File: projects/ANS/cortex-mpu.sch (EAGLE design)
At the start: 26 parts, among them IC1 LM1117MPX-3.3, U1 AT32UC3B164-AUT, Y1 7A-16

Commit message: mpu
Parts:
- added C10, C8: 0.1uF, SparkFun-Passives:CAP0603-CAP
- added C11: 10nF, SparkFun-Passives:CAP0603-CAP
- added C9: 2.2nF, SparkFun-Passives:CAP0603-CAP
- added CLKOUT, E_SCL, E_SDA: (no value), wirepad:1,6/0,8
- added D2, D6: GREEN, SparkFun-LED:LED-GREEN0603
- added LOGO1: OSHW-LOGOS-COPPER, SparkFun-Aesthetics:OSHW-LOGOS-COPPER
- added R10, R9: 150R, SparkFun-Passives:RESISTOR0603-RES
- added R11, R12: 10kR, SparkFun-Passives:RESISTOR0603-RES
- added SJ1, SJ2: SPK, SparkFun-Passives:JUMPER-PAD-2-NC_BY_TRACE
- added SJ3: SPK, SparkFun-Passives:JUMPER-PAD-3-2OF3_NC_BY_TRACE_LARGE
- added U2: (no value), SparkFun-Sensors:MPU-9150QFN-24-NP
- D5: value RED -> GREEN; device SparkFun-LED:LED-RED0603 -> SparkFun-LED:LED-GREEN0603
- R5, R6: value 820R -> 150R
- R7: value (none) -> 150R
- S1: value SWITCH-MOMENTARY-2SMD-4 -> 2SMD-4
- S2: value SWITCH-MOMENTARY-2SMD-4 -> 2SMD4
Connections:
- new net E_SDA: E_SDA.P, U2.E_SDA
- new net GNDANA: U1.GNDANA
- new net N$10: C8.1, U2.REGOUT
- new net N$11: C9.1, U2.CPOUT
- new net N$12: SJ3.2, U2.AD0
- new net N$14: E_SCL.P, U2.E_SCL
- new net N$15: SJ1.2, U2.FSYNC
- new net N$16: CLKOUT.P, U2.CLKOUT
- new net N$6: D5.A, R7.1
- new net N$7: D6.A, R9.1
- new net N$8: D2.A, R10.1
- new net N$9: SJ2.2, U2.CLKIN
- new net VDDANA: U1.VDDANA
- new net VDDCORE: U1.VDDCORE
- new net VDDCORE_2: U1.VDDCORE_2
- new net VDDCORE_3: U1.VDDCORE_3
- new net VDDIN: U1.VDDIN
- new net VDDIO: U1.VDDIO
- new net VDDIO_2: U1.VDDIO_2
- new net VDDIO_3: U1.VDDIO_3
- new net VDDOUT: U1.VDDOUT
- new net VDDPLL: U1.VDDPLL
- net GND: now also C10.2, C11.2, C8.2, C9.2, SJ1.1, SJ2.1, SJ3.3, U2.GND@15, U2.GND@17, U2.GND@18
- net PA10: now also R12.1, U2.SDA
- net PA21: now also D5.C
- net PA22: now also D6.C
- net PA5: now also U2.INT
- net PA7: now also D2.C
- net PA9: now also R11.1, U2.SCL
- net VCC: now also C10.1, C11.1, R10.2, R11.2, R12.2, R7.2, R9.2, SJ3.1, U2.VDD@13, U2.VDD@3, U2.VLOGIC
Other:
- note added: "MPU-9150 I2C/TWI"
- moved on the sheet: C6, C7, D3, D4, D5, R3, R4, R5, R6, R7, S1, S2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

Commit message: vdd
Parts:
- added L1: 3.3uH, SparkFun-Passives:INDUCTOR0603
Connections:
- removed net VDDIO_2: U1.VDDIO_2
- removed net VDDIO_3: U1.VDDIO_3
- net VCC: now also L1.1
- net VDDANA: now also L1.2, U1.ADVREF
- net VDDIO: now also U1.VDDIO_2, U1.VDDIO_3
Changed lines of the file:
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@@
 <part name="GND9" library="SparkFun-Aesthetics" deviceset="GND" device=""/>
 <part name="LOGO1" library="SparkFun-Aesthetics" deviceset="OSHW-LOGO" device="S-COPPER"/>
+<part name="L1" library="SparkFun-Passives" deviceset="INDUCTOR" device="0603" value="3.3uH"/>
+<part name="SUPPLY1" library="SparkFun-Aesthetics" deviceset="VCC" device=""/>
 </parts>
 <sheets>
@@
 <instance part="GND9" gate="1" x="142.24" y="10.16"/>
 <instance part="LOGO1" gate="G$1" x="162.56" y="12.7"/>
+<instance part="L1" gate="G$1" x="12.7" y="43.18"/>
+<instance part="SUPPLY1" gate="G$1" x="12.7" y="53.34"/>
 </instances>
 <busses>
@@
 <wire x1="60.96" y1="38.1" x2="63.5" y2="38.1" width="0.1524" layer="91"/>
 </segment>
+<segment>
+<pinref part="SUPPLY1" gate="G$1" pin="VCC"/>
+<pinref part="L1" gate="G$1" pin="1"/>
+<wire x1="12.7" y1="53.34" x2="12.7" y2="50.8" width="0.1524" layer="91"/>
+</segment>
 </net>
 <net name="N$5" class="0">
@@
 <segment>
 <pinref part="U1" gate="A" pin="VDDANA"/>
-<wire x1="35.56" y1="170.18" x2="30.48" y2="170.18" width="0.1524" layer="91"/>
+<wire x1="35.56" y1="170.18" x2="33.02" y2="170.18" width="0.1524" layer="91"/>
 <label x="20.32" y="170.18" size="1.778" layer="95"/>
+<wire x1="33.02" y1="170.18" x2="30.48" y2="170.18" width="0.1524" layer="91"/>
+<wire x1="33.02" y1="170.18" x2="33.02" y2="142.24" width="0.1524" layer="91"/>
+<junction x="33.02" y="170.18"/>
+<pinref part="U1" gate="A" pin="ADVREF"/>
+<wire x1="33.02" y1="142.24" x2="35.56" y2="142.24" width="0.1524" layer="91"/>
+</segment>
+<segment>
+<wire x1="12.7" y1="33.02" x2="12.7" y2="35.56" width="0.1524" layer="91"/>
+<pinref part="L1" gate="G$1" pin="2"/>
+<label x="7.62" y="33.02" size="1.778" layer="95"/>
 </segment>
 </net>
@@
 <wire x1="35.56" y1="160.02" x2="30.48" y2="160.02" width="0.1524" layer="91"/>
 <label x="20.32" y="160.02" size="1.778" layer="95"/>
-</segment>
-</net>
-<net name="VDDIO_2" class="0">
-<segment>
-<pinref part="U1" gate="A" pin="VDDIO_2"/>
-<wire x1="35.56" y1="157.48" x2="30.48" y2="157.48" width="0.1524" layer="91"/>
-<label x="20.32" y="157.48" size="1.778" layer="95"/>
-</segment>
-</net>
-<net name="VDDIO_3" class="0">
-<segment>
-<pinref part="U1" gate="A" pin="VDDIO_3"/>
-<wire x1="35.56" y1="154.94" x2="30.48" y2="154.94" width="0.1524" layer="91"/>
-<label x="20.32" y="154.94" size="1.778" layer="95"/>
-</segment>
-</net>
-<net name="VDDIO" class="0">
-<segment>
-<pinref part="U1" gate="A" pin="VDDIO"/>
-<wire x1="35.56" y1="152.4" x2="30.48" y2="152.4" width="0.1524" layer="91"/>
-<label x="20.32" y="152.4" size="1.778" layer="95"/>
 </segment>
 </net>
@@
 </segment>
 </net>
+<net name="VDDIO" class="0">
+<segment>
+<pinref part="U1" gate="A" pin="VDDIO_2"/>
+<wire x1="35.56" y1="157.48" x2="30.48" y2="157.48" width="0.1524" layer="91"/>
+<pinref part="U1" gate="A" pin="VDDIO_3"/>
+<wire x1="35.56" y1="154.94" x2="30.48" y2="154.94" width="0.1524" layer="91"/>
+<label x="20.32" y="154.94" size="1.778" layer="95"/>
+<wire x1="30.48" y1="157.48" x2="30.48" y2="154.94" width="0.1524" layer="91"/>
+<pinref part="U1" gate="A" pin="VDDIO"/>
+<wire x1="35.56" y1="152.4" x2="30.48" y2="152.4" width="0.1524" layer="91"/>
+<wire x1="30.48" y1="154.94" x2="30.48" y2="152.4" width="0.1524" layer="91"/>
+<junction x="30.48" y="154.94"/>
+</segment>
+</net>

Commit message: Decoupling
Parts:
- added C12, C13, C14, C15, C16, C17, C18, C19, C20, C21, C22, C23, C24, C25, C26, C27, C28, C29, C30, C31, C32, C33, C34: (no value), SparkFun-Passives:CAP0603-CAP
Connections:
- net GND: now also C12.2, C13.2, C14.2, C15.2, C16.2, C17.2, C18.2, C19.2, C20.2, C21.2, C22.2, C23.2, C24.2, C25.2, C26.2, C27.2, C28.2, C29.2, C30.2, C31.2, C32.2, C33.2, C34.2
- net VDDCORE: now also C25.1, C26.1, C27.1, C28.1, C29.1, C30.1, C31.1, C32.1, C33.1, C34.1
- net VDDIN: now also C23.1, C24.1
- net VDDIO: now also C15.1, C16.1, C17.1, C18.1, C19.1, C20.1
- net VDDOUT: now also C21.1, C22.1
- net VDDPLL: now also C12.1, C13.1, C14.1
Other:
- note added: "Decoupling Capacitors"
- note added: "Filter"
- moved on the sheet: C10, C11, C8, C9, CLKOUT, E_SCL, E_SDA, L1, R11, R12, SJ1, SJ2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

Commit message: Decoupling Capr
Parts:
- added C35: 4.7uF, SparkFun-Passives:CAP0603-CAP
- added C36: 100nF, SparkFun-Passives:CAP0603-CAP
- added C37: 33nF, SparkFun-Passives:CAP0603-CAP
- C12, C25, C26, C27: value (none) -> 2.7nF
- C13, C18, C19, C20, C23, C28, C29, C30: value (none) -> 33nF
- C14: value (none) -> 2.2nF
- C15, C16, C17, C24, C31, C32, C33: value (none) -> 100nF
- C21, C34: value (none) -> 2.2uF
- C22: value (none) -> 470pF
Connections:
- removed net GNDANA: U1.GNDANA
- net GND: now also C35.2, C36.2, C37.2, U1.GNDANA
- net VDDANA: now also C36.1, C37.1
- net VDDIO: now also C35.1
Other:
- moved on the sheet: C10, C11, C18, C19, C20, C8, C9, CLKOUT, E_SCL, E_SDA, R11, R12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

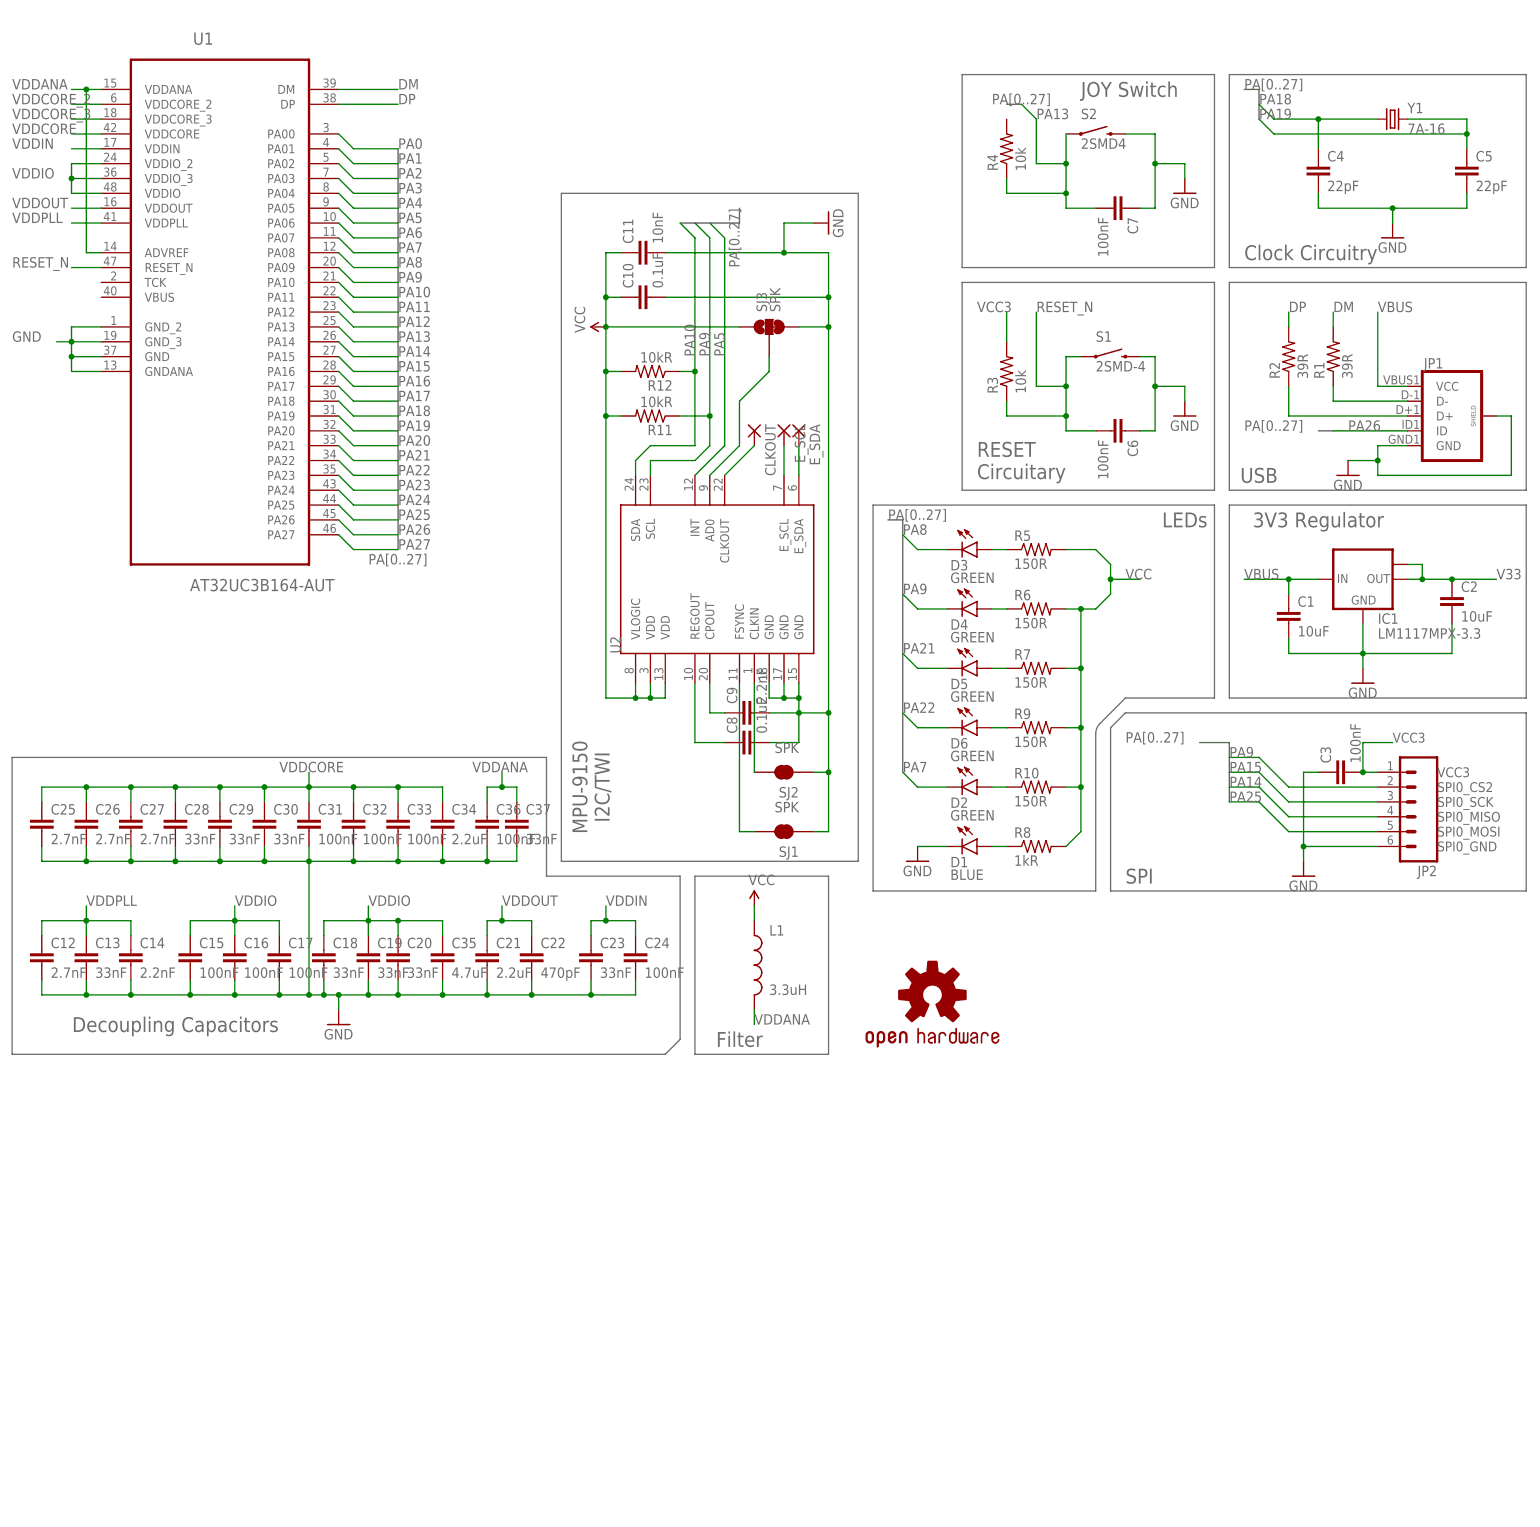
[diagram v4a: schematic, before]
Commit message: Decoupling, Changes
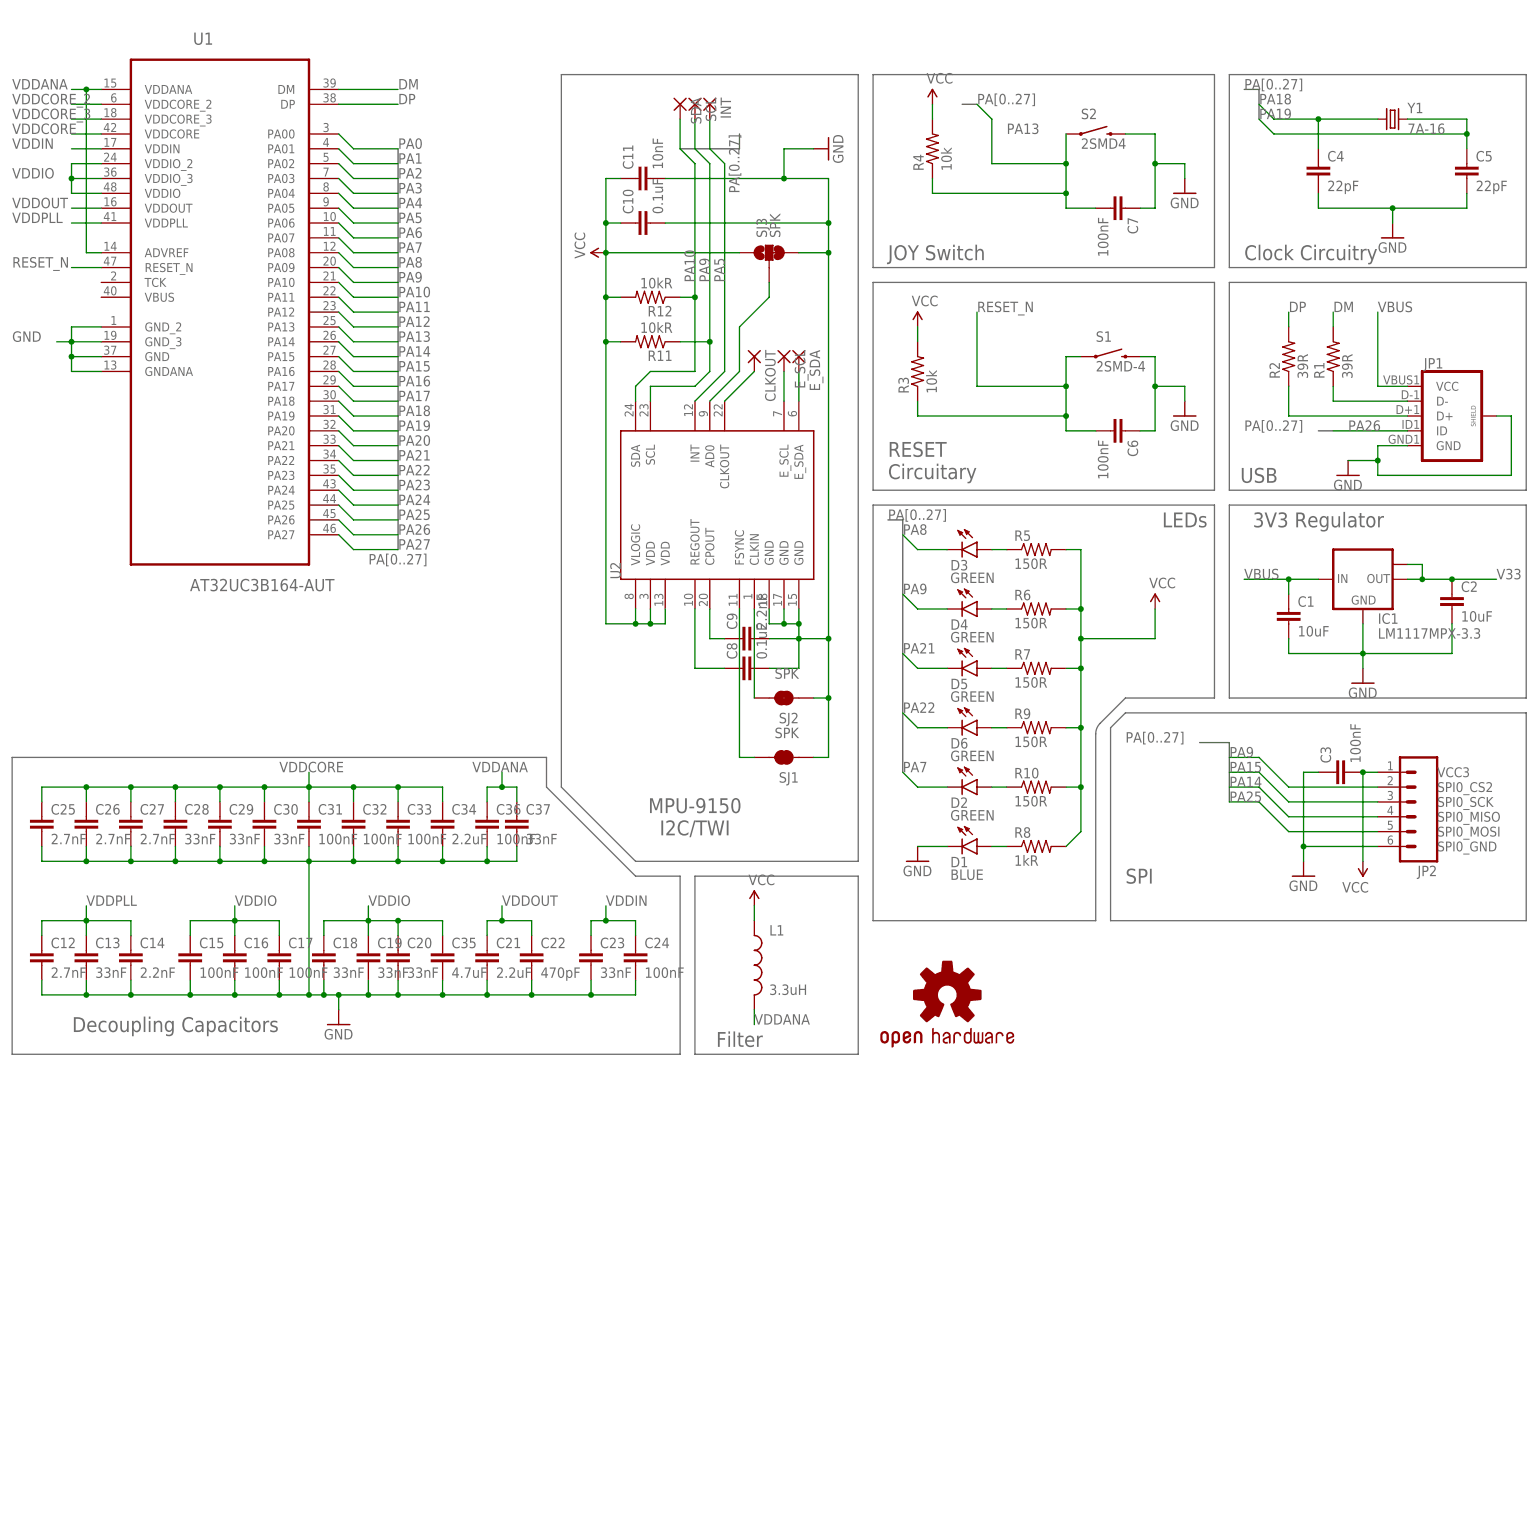
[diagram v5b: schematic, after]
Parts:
- added INT, SCL, SDA: (no value), wirepad:1,6/0,8
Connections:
- removed net VCC3: C3.2, JP2.1, R3.2
- net PA10: now also SDA.P
- net PA5: now also INT.P
- net PA9: now also SCL.P
- net VCC: now also C3.2, JP2.1, R3.2, R4.2
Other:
- moved on the sheet: C10, C11, C8, C9, CLKOUT, E_SCL, E_SDA, R11, R12, R3, R4, SJ1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

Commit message: Pdf
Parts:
- C1, C2: value 10uF -> 2.7nF
- C10, C8: value 0.1uF -> 100nF
- C11: value 10nF -> 33nF
- C12, C26: value 2.7nF -> 100nF
- C13: value 33nF -> 100nF
- C14, C9: value 2.2nF -> 33nF
- C16, C7: value 100nF -> 33nF
- C19: value 33nF -> 2.2uF
- C20: value 33nF -> 4.7uF
- C21: value 2.2uF -> 100nF
- C22: value 470pF -> 2.2uF
- C24: value 100nF -> 470pF
- C25: value 2.7nF -> 33nF
- C27: value 2.7nF -> 10nF
- C28, C30: value 33nF -> 0.1uF
- C29: value 33nF -> 2.2nF
- C3: value 100nF -> 2.7nF
- C33, C36: value 100nF -> 10uF
- C34: value 2.2uF -> 22pF
- C35: value 4.7uF -> 100nF
- C37: value 33nF -> 22pF
- C4: value 22pF -> 33nF
- C5: value 22pF -> 2.7nF
- C6: value 100nF -> 2.2nF
- D1: value BLUE -> GREEN; device SparkFun-LED:LED-BLUE0603 -> SparkFun-LED:LED-GREEN0603
- D6: value GREEN -> BLUE; device SparkFun-LED:LED-GREEN0603 -> SparkFun-LED:LED-BLUE0603
- JP1: device SparkFun-Connectors:USB_MICROB_PLUGCONN-11752 -> SparkFun-Connectors:M06LOCK_LONGPADS
- JP2: device SparkFun-Connectors:M06LOCK_LONGPADS -> SparkFun-Connectors:USB_MICROB_PLUGCONN-11752
- R1, R2: value 39R -> 10kR
- R10: value 150R -> 1kR
- R11, R12: value 10kR -> 39R
- R8: value 1kR -> 150R
- S1: value 2SMD-4 -> 2SMD4
- S2: value 2SMD4 -> 2SMD-4
- SJ1: device SparkFun-Passives:JUMPER-PAD-2-NC_BY_TRACE -> SparkFun-Passives:JUMPER-PAD-3-2OF3_NC_BY_TRACE_LARGE
- SJ3: device SparkFun-Passives:JUMPER-PAD-3-2OF3_NC_BY_TRACE_LARGE -> SparkFun-Passives:JUMPER-PAD-2-NC_BY_TRACE
- renumbered CLKOUT to PAD4, E_SCL to PAD5, E_SDA to PAD6, INT to PAD3, SCL to PAD2, SDA to PAD1
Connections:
- net DM: now also R12.2; no longer R1.2
- net DP: now also R11.2; no longer R2.2
- net GND: now also C3.2, C31.1, C32.1, C35.1, C6.2, C7.2, D6.C, JP1.6, JP2.GND, JP2.SHIELD, SJ1.3, SJ3.1; no longer C3.1, C31.2, C32.2, C35.2, C6.1, C7.1, D1.C, JP1.GND, JP1.SHIELD, JP2.6, SJ1.1, SJ3.3
- net N$1: now also JP2.D-, R12.1; no longer JP1.D-, R1.1
- net N$10: now also C30.1; no longer C8.1
- net N$11: now also C29.1; no longer C9.1
- net N$12: now also SJ1.2; no longer SJ3.2
- net N$15: now also SJ3.2; no longer SJ1.2
- net N$2: now also JP2.D+, R11.1; no longer JP1.D+, R2.1
- net N$3: now also D1.A; no longer D3.A
- net N$4: now also D2.A; no longer D4.A
- net N$5: now also D6.A, R10.1; no longer D1.A, R8.1
- net N$6: now also D3.A; no longer D5.A
- net N$7: now also D4.A, R8.1; no longer D6.A, R9.1
- net N$8: now also D5.A, R9.1; no longer D2.A, R10.1
- net PA10: now also R1.1; no longer R12.1
- net PA13: now also C31.2, S1.1; no longer C7.2, S2.1
- net PA14: now also JP1.4; no longer JP2.4
- net PA15: now also JP1.3; no longer JP2.3
- net PA18: now also C34.1; no longer C4.1
- net PA19: now also C37.1; no longer C5.1
- net PA21: now also D3.C; no longer D5.C
- net PA22: now also D4.C; no longer D6.C
- net PA25: now also JP1.5; no longer JP2.5
- net PA26: now also JP2.ID; no longer JP1.ID
- net PA7: now also D5.C; no longer D2.C
- net PA8: now also D1.C; no longer D3.C
- net PA9: now also D2.C, JP1.2, R2.1; no longer D4.C, JP2.2, R11.1
- net RESET_N: now also C32.2, S2.1; no longer C6.2, S1.1
- net V33: now also C36.1; no longer C2.1
- net VBUS: now also C33.1, JP2.VCC; no longer C1.1, JP1.VCC
- net VCC: now also C27.1, C28.1, C35.2, JP1.1, R1.2, R2.2, SJ1.1; no longer C10.1, C11.1, C3.2, JP2.1, R11.2, R12.2, SJ3.1
- net VDDANA: now also C21.1, C23.1; no longer C36.1, C37.1
- net VDDCORE: now also C1.1, C11.1, C13.1, C15.1, C17.1, C19.1, C3.1, C5.1, C7.1, C9.1; no longer C25.1, C26.1, C27.1, C28.1, C29.1, C30.1, C31.1, C32.1, C33.1, C34.1
- net VDDIN: now also C25.1, C26.1; no longer C23.1, C24.1
- net VDDIO: now also C10.1, C12.1, C14.1, C8.1; no longer C15.1, C17.1, C19.1, C35.1
- net VDDOUT: now also C24.1; no longer C21.1
- net VDDPLL: now also C2.1, C4.1, C6.1; no longer C12.1, C13.1, C14.1
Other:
- moved on the sheet: C1, C10, C11, C12, C13, C14, C15, C16, C17, C18, C19, C2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
